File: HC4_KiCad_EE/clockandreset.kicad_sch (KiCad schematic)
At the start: 19 parts, among them IC15 74HC14, SW2 SW_Push, SW3 SW_Push, SW4 SW_SPDT

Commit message: PortBを4511に、フットプリントの割り付け開始
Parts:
- CP18: footprint Capacitor_THT:C_Disc_D3.0mm_W1.6mm_P2.50mm -> Capacitor_SMD:C_0603_1608Metric
- IC15: footprint Package_DIP:DIP-14_W7.62mm_Socket -> Package_SO:SO-14_5.3x10.2mm_P1.27mm
- renumbered R11 to R18, R12 to R19, R13 to R20, R14 to R21, R15 to R22, R16 to R23, R17 to R24, R18 to R25, R19 to R26
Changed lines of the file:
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@@
 			)
 		)
-		(property "Footprint" "Package_DIP:DIP-14_W7.62mm_Socket"
+		(property "Footprint" "Package_SO:SO-14_5.3x10.2mm_P1.27mm"
 			(at 114.3 90.17 0)
 			(effects
@@
 		(dnp no)
 		(fields_autoplaced yes)
-		(property "Reference" "R13"
+		(property "Reference" "R20"
 			(at 46.99 86.36 90)
 			(effects
@@
 			(project ""
 				(path "/33731ded-38c0-4297-bdd8-92b082f46ff8/3d67359d-c55c-4207-8a6b-ff7c83e276f6"
-					(reference "R13")
+					(reference "R20")
 					(unit 1)
 				)
@@
 		(dnp no)
 		(fields_autoplaced yes)
-		(property "Reference" "R17"
+		(property "Reference" "R24"
 			(at 110.49 116.8399 0)
 			(effects
@@
 			(project ""
 				(path "/33731ded-38c0-4297-bdd8-92b082f46ff8/3d67359d-c55c-4207-8a6b-ff7c83e276f6"
-					(reference "R17")
+					(reference "R24")
 					(unit 1)
 				)
@@
 			)
 		)
-		(property "Footprint" "Package_DIP:DIP-14_W7.62mm_Socket"
+		(property "Footprint" "Package_SO:SO-14_5.3x10.2mm_P1.27mm"
 			(at 68.58 151.13 0)
 			(effects
@@
 		(dnp no)
 		(fields_autoplaced yes)
-		(property "Reference" "#PWR069"
+		(property "Reference" "#PWR072"
 			(at 118.11 116.84 0)
 			(effects
@@
 			(project ""
 				(path "/33731ded-38c0-4297-bdd8-92b082f46ff8/3d67359d-c55c-4207-8a6b-ff7c83e276f6"
-					(reference "#PWR069")
+					(reference "#PWR072")
 					(unit 1)
 				)
@@
 			)
 		)
-		(property "Footprint" "Package_DIP:DIP-14_W7.62mm_Socket"
+		(property "Footprint" "Package_SO:SO-14_5.3x10.2mm_P1.27mm"
 			(at 68.58 92.71 0)
 			(effects
@@
 		(dnp no)
 		(fields_autoplaced yes)
-		(property "Reference" "#PWR063"
+		(property "Reference" "#PWR066"
 			(at 38.1 111.76 0)
 			(effects
@@
 			(project "HC4_KiCad"
 				(path "/33731ded-38c0-4297-bdd8-92b082f46ff8/3d67359d-c55c-4207-8a6b-ff7c83e276f6"
-					(reference "#PWR063")
+					(reference "#PWR066")
 					(unit 1)
 				)
@@
 		(dnp no)
 		(fields_autoplaced yes)
-		(property "Reference" "#PWR066"
+		(property "Reference" "#PWR069"
 			(at 57.15 111.76 0)
 			(effects
@@
 			(project ""
 				(path "/33731ded-38c0-4297-bdd8-92b082f46ff8/3d67359d-c55c-4207-8a6b-ff7c83e276f6"
-					(reference "#PWR066")
+					(reference "#PWR069")
 					(unit 1)
 				)
@@
 			)
 		)
-		(property "Footprint" "Capacitor_THT:C_Disc_D3.0mm_W1.6mm_P2.50mm"
+		(property "Footprint" "Capacitor_SMD:C_0603_1608Metric"
 			(at 141.9352 180.34 0)
 			(effects
@@
 		(dnp no)
 		(fields_autoplaced yes)
-		(property "Reference" "#PWR067"
+		(property "Reference" "#PWR070"
 			(at 57.15 170.18 0)
 			(effects
@@
 			(project "HC4_KiCad"
 				(path "/33731ded-38c0-4297-bdd8-92b082f46ff8/3d67359d-c55c-4207-8a6b-ff7c83e276f6"
-					(reference "#PWR067")
+					(reference "#PWR070")
 					(unit 1)
 				)
@@
 		(on_board yes)
 		(dnp no)
-		(property "Reference" "R11"
+		(property "Reference" "R18"
 			(at 35.56 86.3599 0)
 			(effects
@@
 			(project "HC4_KiCad"
 				(path "/33731ded-38c0-4297-bdd8-92b082f46ff8/3d67359d-c55c-4207-8a6b-ff7c83e276f6"
-					(reference "R11")
+					(reference "R18")
 					(unit 1)
 				)
@@
 		(dnp no)
 		(fields_autoplaced yes)
-		(property "Reference" "#PWR065"
+		(property "Reference" "#PWR068"
 			(at 38.1 170.18 0)
 			(effects
@@
 			(project ""
 				(path "/33731ded-38c0-4297-bdd8-92b082f46ff8/3d67359d-c55c-4207-8a6b-ff7c83e276f6"
-					(reference "#PWR065")
+					(reference "#PWR068")
 					(unit 1)
 				)
@@
 		(on_board yes)
 		(dnp no)
-		(property "Reference" "R12"
+		(property "Reference" "R19"
 			(at 35.56 144.7799 0)
 			(effects
@@
 			(project ""
 				(path "/33731ded-38c0-4297-bdd8-92b082f46ff8/3d67359d-c55c-4207-8a6b-ff7c83e276f6"
-					(reference "R12")
+					(reference "R19")
 					(unit 1)
 				)
@@
 		(dnp no)
 		(fields_autoplaced yes)
-		(property "Reference" "#PWR068"
+		(property "Reference" "#PWR071"
 			(at 107.95 116.84 0)
 			(effects
@@
 			(project "HC4_KiCad"
 				(path "/33731ded-38c0-4297-bdd8-92b082f46ff8/3d67359d-c55c-4207-8a6b-ff7c83e276f6"
-					(reference "#PWR068")
+					(reference "#PWR071")
 					(unit 1)
 				)
@@
 		(dnp no)
 		(fields_autoplaced yes)
-		(property "Reference" "R16"
+		(property "Reference" "R23"
 			(at 95.25 83.82 90)
 			(effects
@@
 			(project "HC4_KiCad"
 				(path "/33731ded-38c0-4297-bdd8-92b082f46ff8/3d67359d-c55c-4207-8a6b-ff7c83e276f6"
-					(reference "R16")
+					(reference "R23")
 					(unit 1)
 				)
@@
 		(dnp no)
 		(fields_autoplaced yes)
-		(property "Reference" "R14"
+		(property "Reference" "R21"
 			(at 48.26 144.78 90)
 			(effects
@@
 			(project "HC4_KiCad"
 				(path "/33731ded-38c0-4297-bdd8-92b082f46ff8/3d67359d-c55c-4207-8a6b-ff7c83e276f6"
-					(reference "R14")
+					(reference "R21")
 					(unit 1)
 				)
@@
 		(dnp no)
 		(fields_autoplaced yes)
-		(property "Reference" "R19"
+		(property "Reference" "R26"
 			(at 128.27 83.82 90)
 			(effects
@@
 			(project "HC4_KiCad"
 				(path "/33731ded-38c0-4297-bdd8-92b082f46ff8/3d67359d-c55c-4207-8a6b-ff7c83e276f6"
-					(reference "R19")
+					(reference "R26")
 					(unit 1)
 				)
@@
 			)
 		)
-		(property "Footprint" "Package_DIP:DIP-14_W7.62mm_Socket"
+		(property "Footprint" "Package_SO:SO-14_5.3x10.2mm_P1.27mm"
 			(at 64.77 63.5 0)
 			(effects
@@
 		(dnp no)
 		(fields_autoplaced yes)
-		(property "Reference" "#PWR064"
+		(property "Reference" "#PWR067"
 			(at 38.1 144.78 0)
 			(effects
@@
 			(project ""
 				(path "/33731ded-38c0-4297-bdd8-92b082f46ff8/3d67359d-c55c-4207-8a6b-ff7c83e276f6"
-					(reference "#PWR064")
+					(reference "#PWR067")
 					(unit 1)
 				)
@@
 			)
 		)
-		(property "Footprint" "Package_DIP:DIP-14_W7.62mm_Socket"
+		(property "Footprint" "Package_SO:SO-14_5.3x10.2mm_P1.27mm"
 			(at 156.21 176.53 0)
 			(effects
@@
 		(dnp no)
 		(fields_autoplaced yes)
-		(property "Reference" "#PWR062"
+		(property "Reference" "#PWR065"
 			(at 38.1 86.36 0)
 			(effects
@@
 			(project "HC4_KiCad"
 				(path "/33731ded-38c0-4297-bdd8-92b082f46ff8/3d67359d-c55c-4207-8a6b-ff7c83e276f6"
-					(reference "#PWR062")
+					(reference "#PWR065")
 					(unit 1)
 				)
@@
 		(dnp no)
 		(fields_autoplaced yes)
-		(property "Reference" "R18"
+		(property "Reference" "R25"
 			(at 120.65 116.8399 0)
 			(effects
@@
 			(project "HC4_KiCad"
 				(path "/33731ded-38c0-4297-bdd8-92b082f46ff8/3d67359d-c55c-4207-8a6b-ff7c83e276f6"
-					(reference "R18")
+					(reference "R25")
 					(unit 1)
 				)
@@
 			)
 		)
-		(property "Footprint" "Package_DIP:DIP-14_W7.62mm_Socket"
+		(property "Footprint" "Package_SO:SO-14_5.3x10.2mm_P1.27mm"
 			(at 46.99 63.5 0)
 			(effects
@@
 			)
 		)
-		(property "Footprint" "Package_DIP:DIP-14_W7.62mm_Socket"
+		(property "Footprint" "Package_SO:SO-14_5.3x10.2mm_P1.27mm"
 			(at 85.09 151.13 0)
 			(effects
@@
 		(dnp no)
 		(fields_autoplaced yes)
-		(property "Reference" "#PWR071"
+		(property "Reference" "#PWR074"
 			(at 156.21 196.85 0)
 			(effects
@@
 			(project ""
 				(path "/33731ded-38c0-4297-bdd8-92b082f46ff8/3d67359d-c55c-4207-8a6b-ff7c83e276f6"
-					(reference "#PWR071")
+					(reference "#PWR074")
 					(unit 1)
 				)
@@
 		(dnp no)
 		(fields_autoplaced yes)
-		(property "Reference" "#PWR070"
+		(property "Reference" "#PWR073"
 			(at 156.21 166.37 0)
 			(effects
@@
 			(project ""
 				(path "/33731ded-38c0-4297-bdd8-92b082f46ff8/3d67359d-c55c-4207-8a6b-ff7c83e276f6"
-					(reference "#PWR070")
+					(reference "#PWR073")
 					(unit 1)
 				)
@@
 		(dnp no)
 		(fields_autoplaced yes)
-		(property "Reference" "R15"
+		(property "Reference" "R22"
 			(at 58.42 48.2599 0)
 			(effects
@@
 			(project ""
 				(path "/33731ded-38c0-4297-bdd8-92b082f46ff8/3d67359d-c55c-4207-8a6b-ff7c83e276f6"
-					(reference "R15")
-					(unit 1)
-				)
+					(reference "R22")
+					(unit 1)
+				)

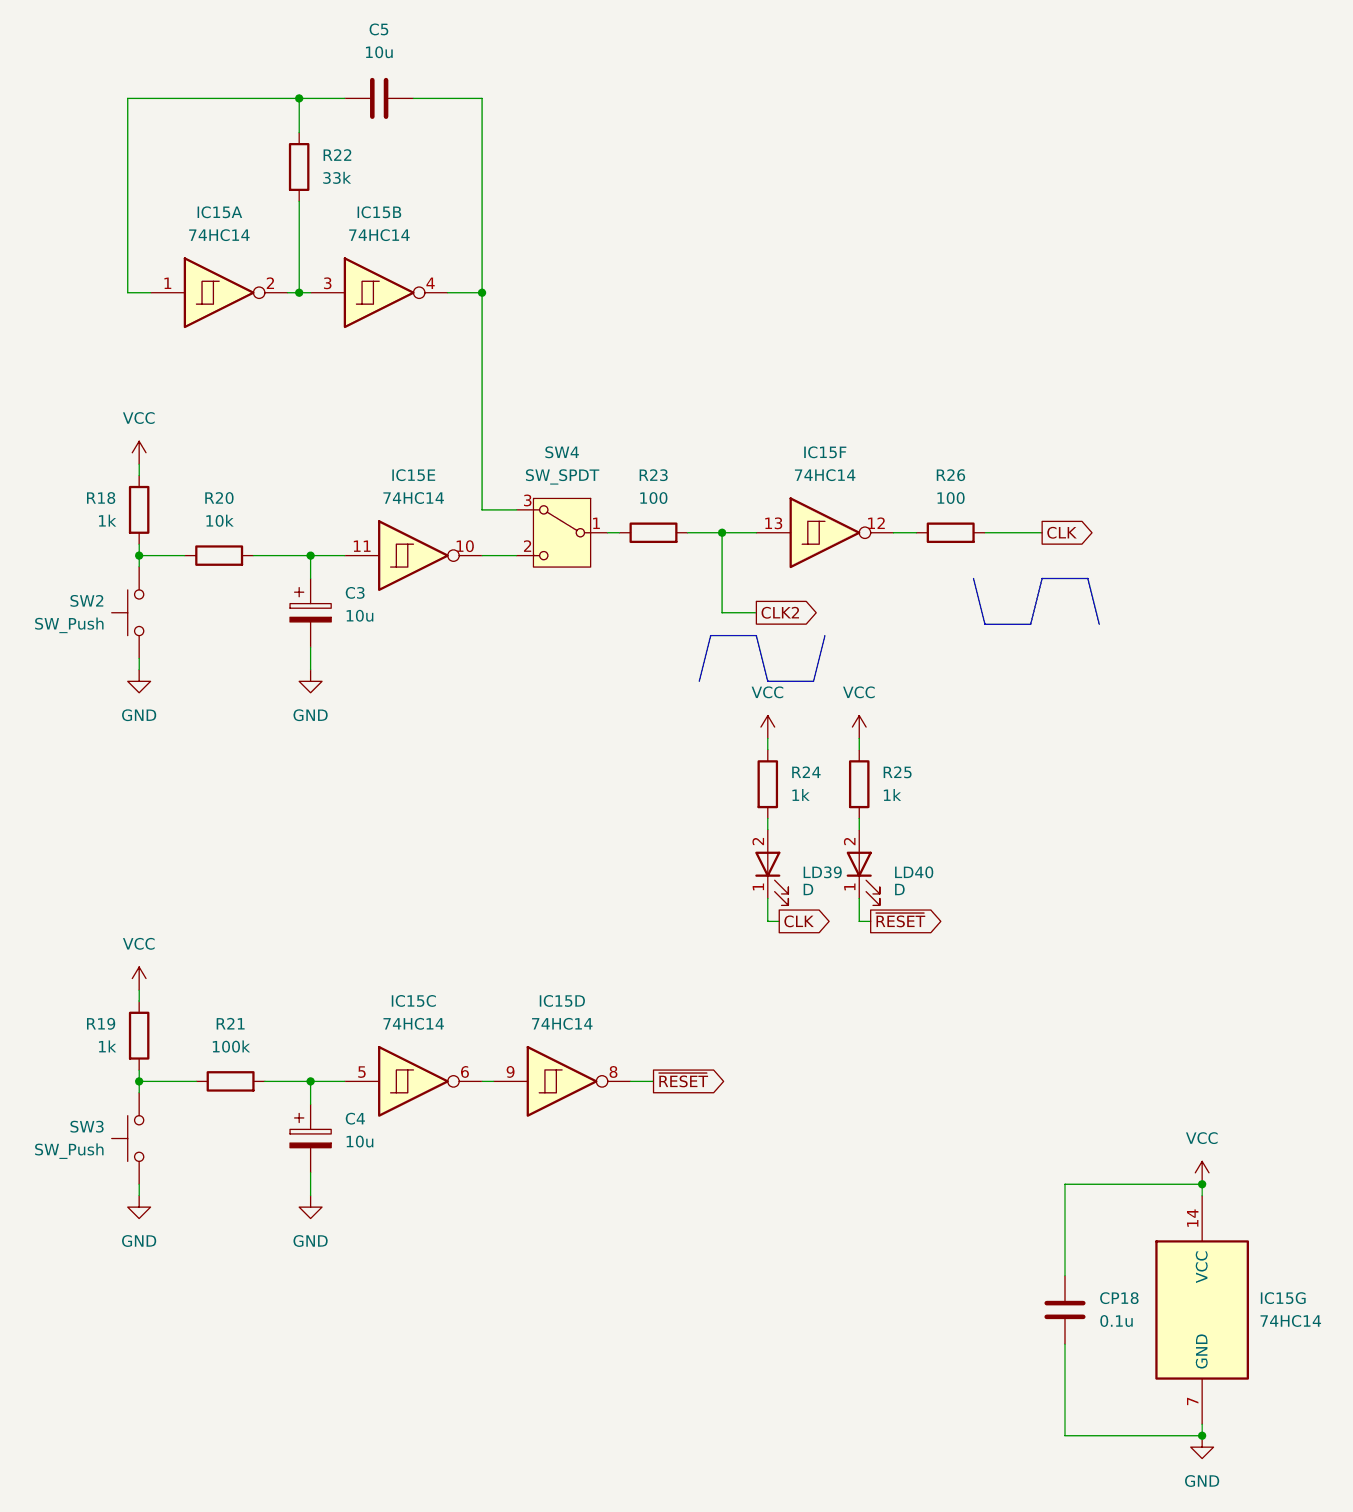
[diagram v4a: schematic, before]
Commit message: チップ集合抵抗に変更、基板作成開始
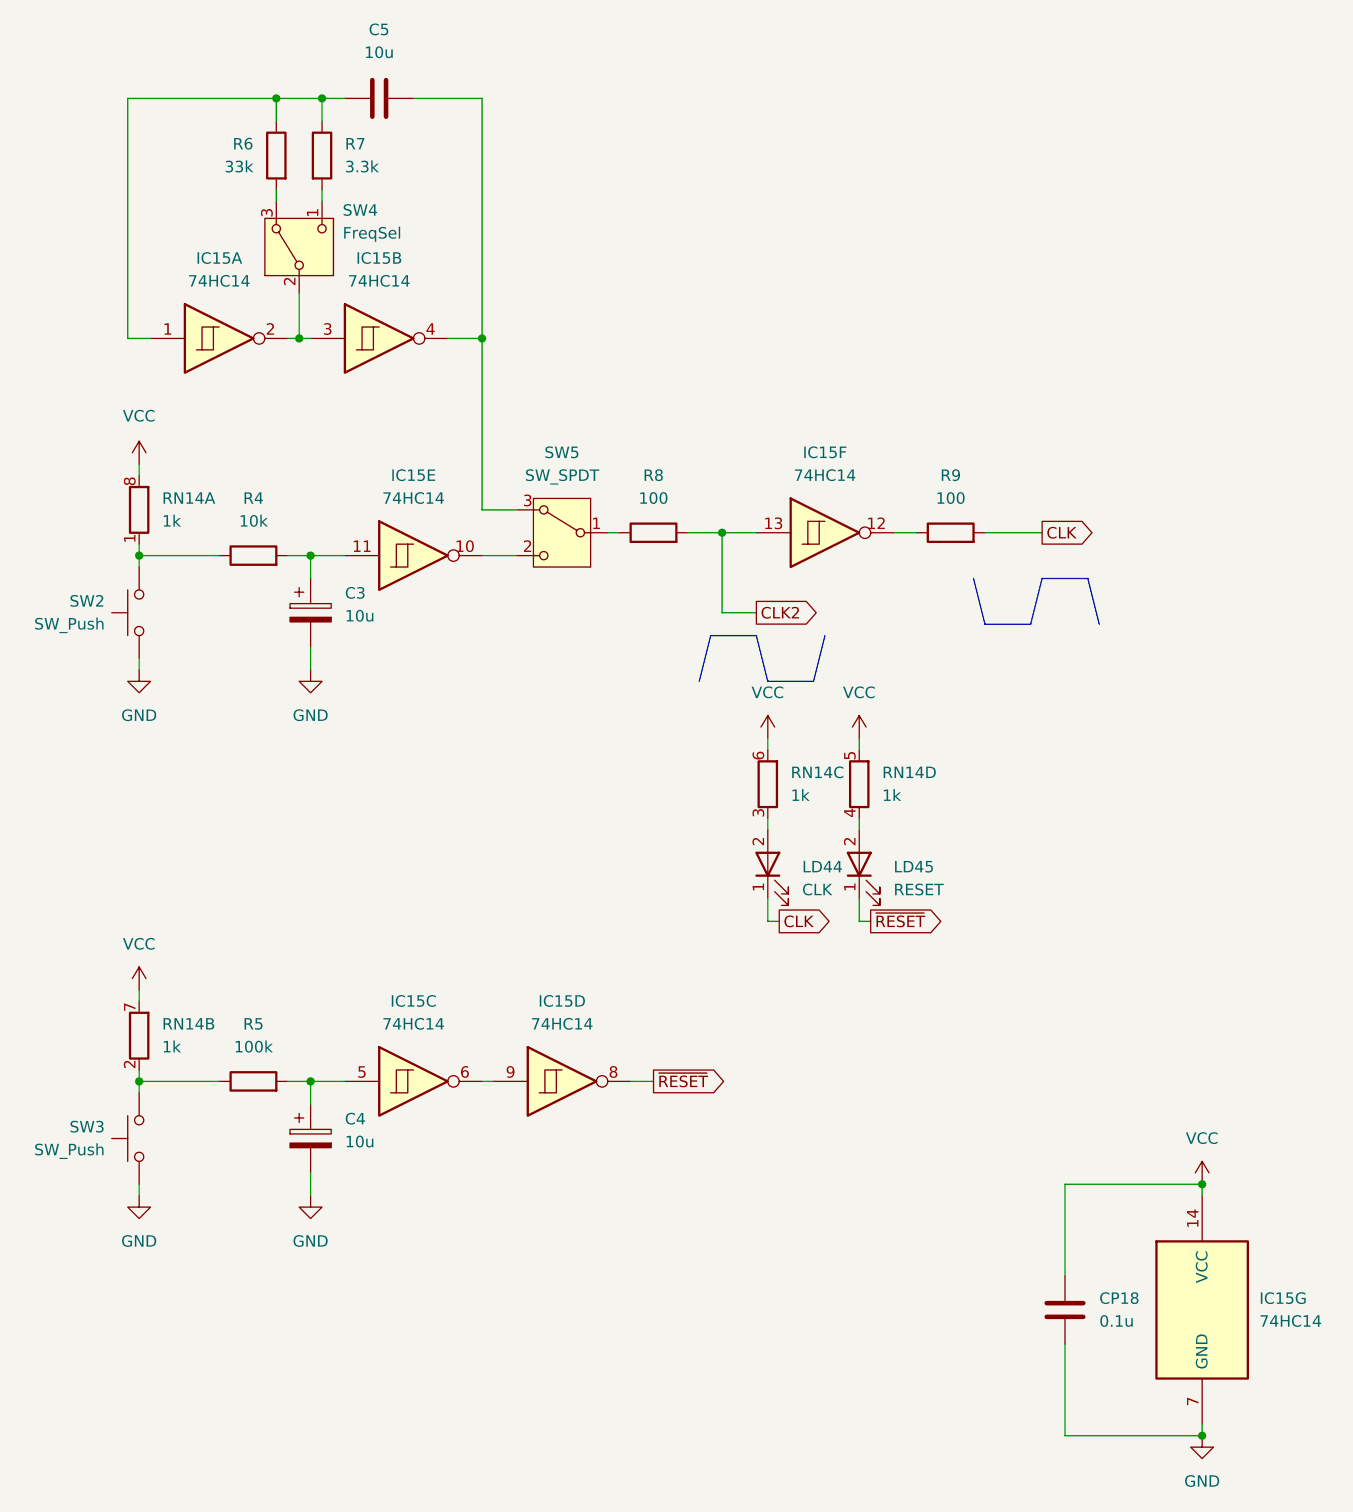
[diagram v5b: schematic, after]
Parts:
- removed R18, R19, R24, R25: 1k, Resistor_THT:R_Axial_DIN0207_L6.3mm_D2.5mm_P7.62mm_Horizontal, symbol Device:R
- added R7: 3.3k, Resistor_SMD:R_0603_1608Metric, symbol Device:R
- added RN14: 1k, Resistor_SMD:R_Array_Convex_4x0603, symbol Device:R_Pack04_Split
- added SW4: FreqSel, Button_Switch_THT:SW_Slide-03_Wuerth-WS-SLTV_10x2.5x6.4_P2.54mm, symbol Switch:SW_SPDT_321
- LD44: renamed from LD39; value D -> CLK
- LD45: renamed from LD40; value D -> RESET
- R4: renamed from R20; footprint Resistor_THT:R_Axial_DIN0207_L6.3mm_D2.5mm_P7.62mm_Horizontal -> Resistor_SMD:R_0603_1608Metric
- R5: renamed from R21; footprint Resistor_THT:R_Axial_DIN0207_L6.3mm_D2.5mm_P7.62mm_Horizontal -> Resistor_SMD:R_0603_1608Metric
- R6: renamed from R22; footprint Resistor_THT:R_Axial_DIN0207_L6.3mm_D2.5mm_P7.62mm_Horizontal -> Resistor_SMD:R_0603_1608Metric
- R8: renamed from R23; footprint Resistor_THT:R_Axial_DIN0207_L6.3mm_D2.5mm_P7.62mm_Horizontal -> Resistor_SMD:R_0603_1608Metric
- R9: renamed from R26; footprint Resistor_THT:R_Axial_DIN0207_L6.3mm_D2.5mm_P7.62mm_Horizontal -> Resistor_SMD:R_0603_1608Metric
- renumbered SW4 to SW5
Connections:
- net VCC: now also RN14.5 (R4.2), RN14.6 (R3.2), RN14.7 (R2.2), RN14.8 (R1.2)
- net at R4.1, SW2.2: now also RN14.1 (R1.1)
- net at LD44.2: now also RN14.3 (R3.1)
- net at C5.1, IC15.1, R6.1: now also R7.1
- net at R5.1, SW3.2: now also RN14.2 (R2.1)
- net at LD45.2: now also RN14.4 (R4.1)
- net at IC15.2, IC15.3: now also SW4.2 (B); no longer R6.2
- new net: R7.2, SW4.1 (C)
- new net: R6.2, SW4.3 (A)
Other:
- moved on the sheet: IC15A, IC15B, R4, R5, R6
